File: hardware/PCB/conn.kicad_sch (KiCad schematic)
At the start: 19 parts, among them J3 Motor1, J4 Motor2, J5 Motor3, J6 6V, J7 SJ-3523-SMT-TR, Q1 2N3904, Q2 2N3904, SW3 PWR

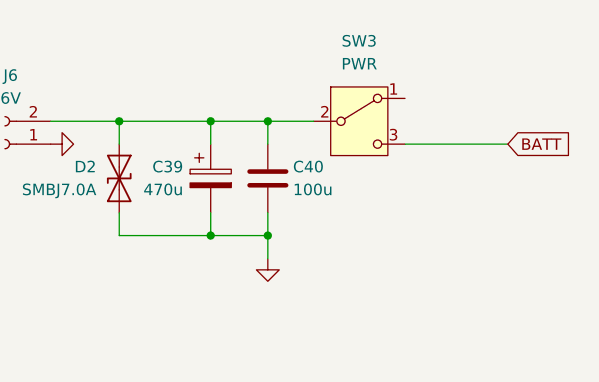
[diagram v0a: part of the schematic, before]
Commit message: Added connection for external IMU to PCB
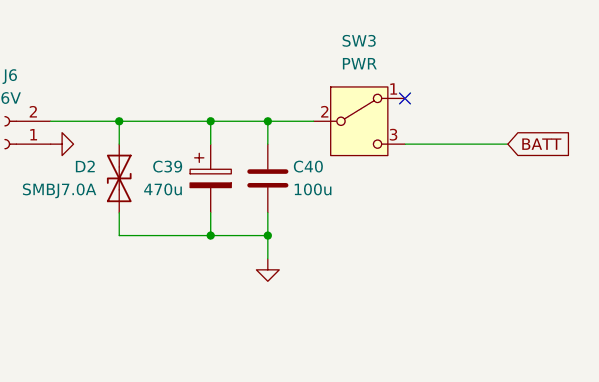
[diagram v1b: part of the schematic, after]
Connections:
- no-connect marks 0 -> 1
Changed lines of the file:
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@@
 		(color 0 0 0 0)
+	)
+	(no_connect
+		(at 173.99 30.48)
 	)
 	(wire

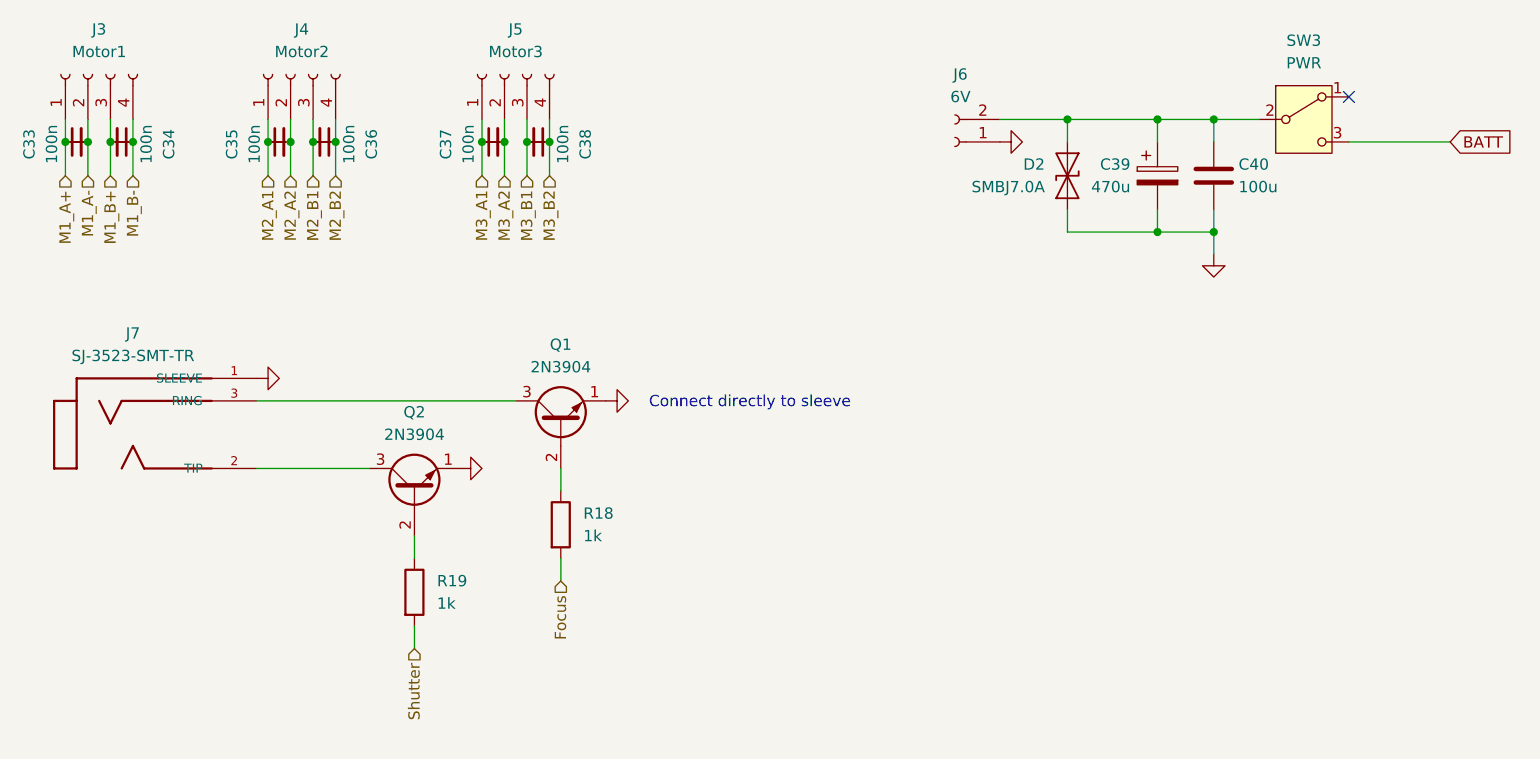
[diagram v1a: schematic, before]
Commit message: Finished schematic for LoRa, added BME280
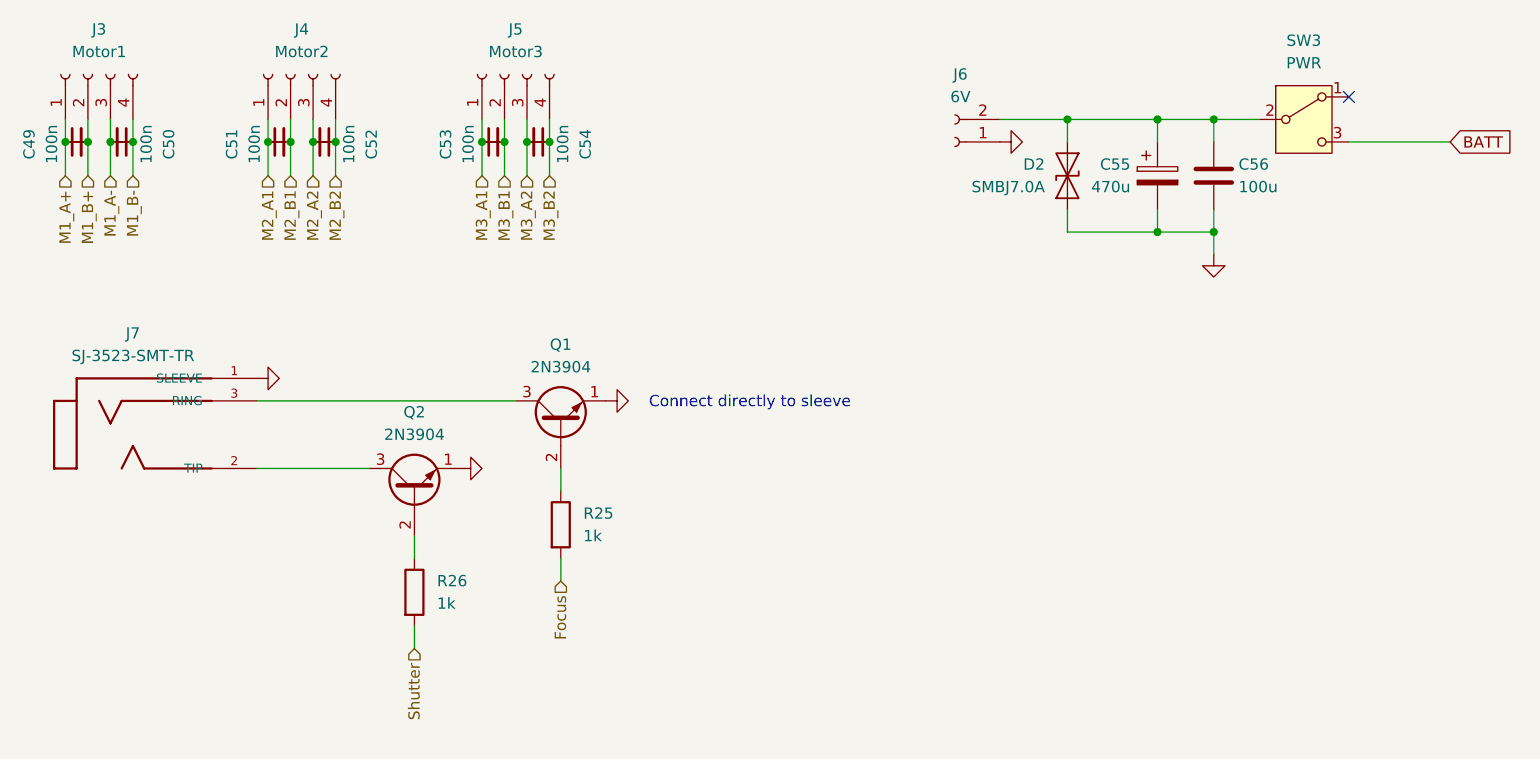
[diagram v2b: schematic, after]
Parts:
- renumbered C33 to C49, C34 to C50, C35 to C51, C36 to C52, C37 to C53, C38 to C54, C39 to C55, C40 to C56, R18 to R25, R19 to R26
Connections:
- net M1_A-: now also C50.2, J3.3 (Pin_3); no longer C49.2, J3.2 (Pin_2)
- net M1_B+: now also C49.2, J3.2 (Pin_2); no longer C50.2, J3.3 (Pin_3)
- net M2_A2: now also C52.2, J4.3 (Pin_3); no longer C51.2, J4.2 (Pin_2)
- net M2_B1: now also C51.2, J4.2 (Pin_2); no longer C52.2, J4.3 (Pin_3)
- net M3_A2: now also C54.2, J5.3 (Pin_3); no longer C53.2, J5.2 (Pin_2)
- net M3_B1: now also C53.2, J5.2 (Pin_2); no longer C54.2, J5.3 (Pin_3)
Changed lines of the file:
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@@
 	(hierarchical_label "M3_A2"
 		(shape input)
-		(at 78.74 39.37 270)
+		(at 81.28 39.37 270)
 		(effects
 			(font
@@
 	(hierarchical_label "M1_B+"
 		(shape input)
-		(at 34.29 39.37 270)
+		(at 31.75 39.37 270)
 		(effects
 			(font
@@
 	(hierarchical_label "M1_A-"
 		(shape input)
-		(at 31.75 39.37 270)
+		(at 34.29 39.37 270)
 		(effects
 			(font
@@
 	(hierarchical_label "M2_A2"
 		(shape input)
-		(at 54.61 39.37 270)
+		(at 57.15 39.37 270)
 		(effects
 			(font
@@
 	(hierarchical_label "M3_B1"
 		(shape input)
-		(at 81.28 39.37 270)
+		(at 78.74 39.37 270)
 		(effects
 			(font
@@
 	(hierarchical_label "M2_B1"
 		(shape input)
-		(at 57.15 39.37 270)
+		(at 54.61 39.37 270)
 		(effects
 			(font
@@
 		(on_board yes)
 		(dnp no)
-		(property "Reference" "C39"
+		(property "Reference" "C55"
 			(at 149.352 38.1 0)
 			(effects
@@
 			(project ""
 				(path "/45ea479c-a8ef-4c14-88b0-391ede4fd156/1d933153-cc32-40aa-bf24-5d7da12d1a94"
-					(reference "C39")
+					(reference "C55")
 					(unit 1)
 				)
@@
 		(on_board yes)
 		(dnp no)
-		(property "Reference" "C36"
+		(property "Reference" "C52"
 			(at 63.754 35.814 0)
 			(effects
@@
 			(project "Startracker"
 				(path "/45ea479c-a8ef-4c14-88b0-391ede4fd156/1d933153-cc32-40aa-bf24-5d7da12d1a94"
-					(reference "C36")
+					(reference "C52")
 					(unit 1)
 				)
@@
 		(on_board yes)
 		(dnp no)
-		(property "Reference" "C40"
+		(property "Reference" "C56"
 			(at 161.544 38.1 0)
 			(effects
@@
 			(project ""
 				(path "/45ea479c-a8ef-4c14-88b0-391ede4fd156/1d933153-cc32-40aa-bf24-5d7da12d1a94"
-					(reference "C40")
+					(reference "C56")
 					(unit 1)
 				)
@@
 		(on_board yes)
 		(dnp no)
-		(property "Reference" "C33"
+		(property "Reference" "C49"
 			(at 25.146 35.814 0)
 			(effects
@@
 			(project ""
 				(path "/45ea479c-a8ef-4c14-88b0-391ede4fd156/1d933153-cc32-40aa-bf24-5d7da12d1a94"
-					(reference "C33")
+					(reference "C49")
 					(unit 1)
 				)
@@
 		(dnp no)
 		(fields_autoplaced yes)
-		(property "Reference" "R18"
+		(property "Reference" "R25"
 			(at 87.63 77.4699 0)
 			(effects
@@
 			(project ""
 				(path "/45ea479c-a8ef-4c14-88b0-391ede4fd156/1d933153-cc32-40aa-bf24-5d7da12d1a94"
-					(reference "R18")
+					(reference "R25")
 					(unit 1)
 				)
@@
 		(dnp no)
 		(fields_autoplaced yes)
-		(property "Reference" "#PWR068"
+		(property "Reference" "#PWR0103"
 			(at 158.75 54.61 0)
 			(effects
@@
 			(project ""
 				(path "/45ea479c-a8ef-4c14-88b0-391ede4fd156/1d933153-cc32-40aa-bf24-5d7da12d1a94"
-					(reference "#PWR068")
+					(reference "#PWR0103")
 					(unit 1)
 				)
@@
 		(on_board yes)
 		(dnp no)
-		(property "Reference" "C34"
+		(property "Reference" "C50"
 			(at 40.894 35.814 0)
 			(effects
@@
 			(project "Startracker"
 				(path "/45ea479c-a8ef-4c14-88b0-391ede4fd156/1d933153-cc32-40aa-bf24-5d7da12d1a94"
-					(reference "C34")
+					(reference "C50")
 					(unit 1)
 				)
@@
 		(dnp no)
 		(fields_autoplaced yes)
-		(property "Reference" "#PWR067"
+		(property "Reference" "#PWR0102"
 			(at 140.97 35.56 0)
 			(effects
@@
 			(project "Startracker"
 				(path "/45ea479c-a8ef-4c14-88b0-391ede4fd156/1d933153-cc32-40aa-bf24-5d7da12d1a94"
-					(reference "#PWR067")
+					(reference "#PWR0102")
 					(unit 1)
 				)
@@
 		(dnp no)
 		(fields_autoplaced yes)
-		(property "Reference" "#PWR070"
+		(property "Reference" "#PWR0105"
 			(at 96.52 64.77 0)
 			(effects
@@
 			(project "Startracker"
 				(path "/45ea479c-a8ef-4c14-88b0-391ede4fd156/1d933153-cc32-40aa-bf24-5d7da12d1a94"
-					(reference "#PWR070")
+					(reference "#PWR0105")
 					(unit 1)
 				)
@@
 		(dnp no)
 		(fields_autoplaced yes)
-		(property "Reference" "#PWR071"
+		(property "Reference" "#PWR0106"
 			(at 80.01 72.39 0)
 			(effects
@@
 			(project "Startracker"
 				(path "/45ea479c-a8ef-4c14-88b0-391ede4fd156/1d933153-cc32-40aa-bf24-5d7da12d1a94"
-					(reference "#PWR071")
+					(reference "#PWR0106")
 					(unit 1)
 				)
@@
 		(dnp no)
 		(fields_autoplaced yes)
-		(property "Reference" "#PWR069"
+		(property "Reference" "#PWR0104"
 			(at 57.15 62.23 0)
 			(effects
@@
 			(project "Startracker"
 				(path "/45ea479c-a8ef-4c14-88b0-391ede4fd156/1d933153-cc32-40aa-bf24-5d7da12d1a94"
-					(reference "#PWR069")
+					(reference "#PWR0104")
 					(unit 1)
 				)
@@
 		(on_board yes)
 		(dnp no)
-		(property "Reference" "C35"
+		(property "Reference" "C51"
 			(at 48.006 35.814 0)
 			(effects
@@
 			(project "Startracker"
 				(path "/45ea479c-a8ef-4c14-88b0-391ede4fd156/1d933153-cc32-40aa-bf24-5d7da12d1a94"
-					(reference "C35")
+					(reference "C51")
 					(unit 1)
 				)
@@
 		(on_board yes)
 		(dnp no)
-		(property "Reference" "C37"
+		(property "Reference" "C53"
 			(at 72.136 35.814 0)
 			(effects
@@
 			(project "Startracker"
 				(path "/45ea479c-a8ef-4c14-88b0-391ede4fd156/1d933153-cc32-40aa-bf24-5d7da12d1a94"
-					(reference "C37")
+					(reference "C53")
 					(unit 1)
 				)
@@
 		(on_board yes)
 		(dnp no)
-		(property "Reference" "C38"
+		(property "Reference" "C54"
 			(at 87.884 35.814 0)
 			(effects
@@
 			(project "Startracker"
 				(path "/45ea479c-a8ef-4c14-88b0-391ede4fd156/1d933153-cc32-40aa-bf24-5d7da12d1a94"
-					(reference "C38")
+					(reference "C54")
 					(unit 1)
 				)
@@
 		(dnp no)
 		(fields_autoplaced yes)
-		(property "Reference" "R19"
+		(property "Reference" "R26"
 			(at 71.12 85.0899 0)
 			(effects
@@
 			(project "Startracker"
 				(path "/45ea479c-a8ef-4c14-88b0-391ede4fd156/1d933153-cc32-40aa-bf24-5d7da12d1a94"
-					(reference "R19")
-					(unit 1)
-				)
+					(reference "R26")
+					(unit 1)
+				)

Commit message: Finished parts sourcing and added missing footprints
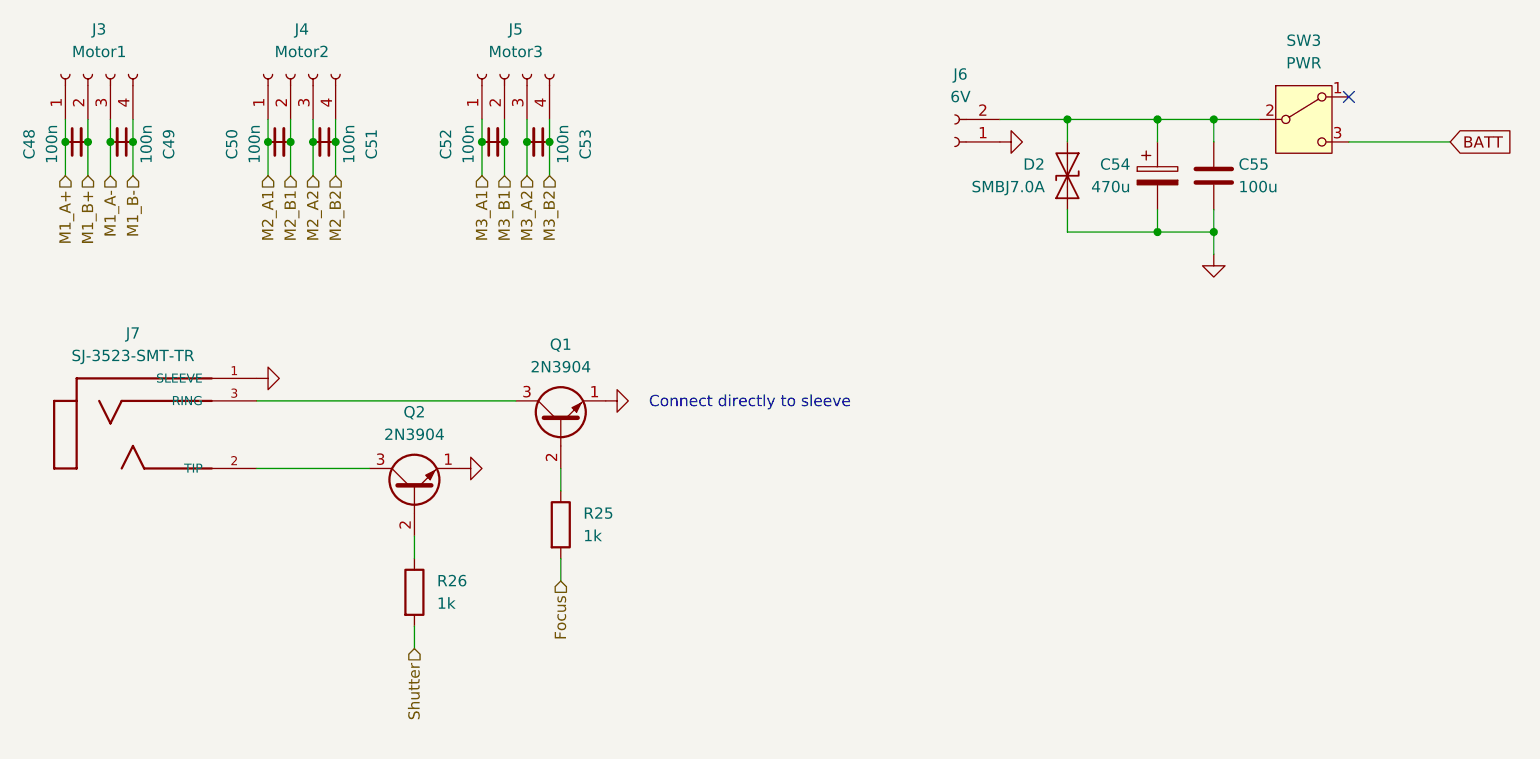
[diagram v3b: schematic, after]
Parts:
- renumbered C49 to C48, C50 to C49, C51 to C50, C52 to C51, C53 to C52, C54 to C53, C55 to C54, C56 to C55
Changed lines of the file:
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@@
 		(on_board yes)
 		(dnp no)
-		(property "Reference" "C55"
+		(property "Reference" "C54"
 			(at 149.352 38.1 0)
 			(effects
@@
 			(project ""
 				(path "/45ea479c-a8ef-4c14-88b0-391ede4fd156/1d933153-cc32-40aa-bf24-5d7da12d1a94"
-					(reference "C55")
+					(reference "C54")
 					(unit 1)
 				)
@@
 		(on_board yes)
 		(dnp no)
-		(property "Reference" "C52"
+		(property "Reference" "C51"
 			(at 63.754 35.814 0)
 			(effects
@@
 			(project "Startracker"
 				(path "/45ea479c-a8ef-4c14-88b0-391ede4fd156/1d933153-cc32-40aa-bf24-5d7da12d1a94"
-					(reference "C52")
+					(reference "C51")
 					(unit 1)
 				)
@@
 		(on_board yes)
 		(dnp no)
-		(property "Reference" "C56"
+		(property "Reference" "C55"
 			(at 161.544 38.1 0)
 			(effects
@@
 			(project ""
 				(path "/45ea479c-a8ef-4c14-88b0-391ede4fd156/1d933153-cc32-40aa-bf24-5d7da12d1a94"
-					(reference "C56")
+					(reference "C55")
 					(unit 1)
 				)
@@
 		(on_board yes)
 		(dnp no)
-		(property "Reference" "C49"
+		(property "Reference" "C48"
 			(at 25.146 35.814 0)
 			(effects
@@
 			(project ""
 				(path "/45ea479c-a8ef-4c14-88b0-391ede4fd156/1d933153-cc32-40aa-bf24-5d7da12d1a94"
-					(reference "C49")
+					(reference "C48")
 					(unit 1)
 				)
@@
 		(on_board yes)
 		(dnp no)
-		(property "Reference" "C50"
+		(property "Reference" "C49"
 			(at 40.894 35.814 0)
 			(effects
@@
 			(project "Startracker"
 				(path "/45ea479c-a8ef-4c14-88b0-391ede4fd156/1d933153-cc32-40aa-bf24-5d7da12d1a94"
-					(reference "C50")
+					(reference "C49")
 					(unit 1)
 				)
@@
 		(on_board yes)
 		(dnp no)
-		(property "Reference" "C51"
+		(property "Reference" "C50"
 			(at 48.006 35.814 0)
 			(effects
@@
 			(project "Startracker"
 				(path "/45ea479c-a8ef-4c14-88b0-391ede4fd156/1d933153-cc32-40aa-bf24-5d7da12d1a94"
-					(reference "C51")
+					(reference "C50")
 					(unit 1)
 				)
@@
 		(on_board yes)
 		(dnp no)
-		(property "Reference" "C53"
+		(property "Reference" "C52"
 			(at 72.136 35.814 0)
 			(effects
@@
 			(project "Startracker"
 				(path "/45ea479c-a8ef-4c14-88b0-391ede4fd156/1d933153-cc32-40aa-bf24-5d7da12d1a94"
-					(reference "C53")
+					(reference "C52")
 					(unit 1)
 				)
@@
 		(on_board yes)
 		(dnp no)
-		(property "Reference" "C54"
+		(property "Reference" "C53"
 			(at 87.884 35.814 0)
 			(effects
@@
 			(project "Startracker"
 				(path "/45ea479c-a8ef-4c14-88b0-391ede4fd156/1d933153-cc32-40aa-bf24-5d7da12d1a94"
-					(reference "C54")
-					(unit 1)
-				)
+					(reference "C53")
+					(unit 1)
+				)

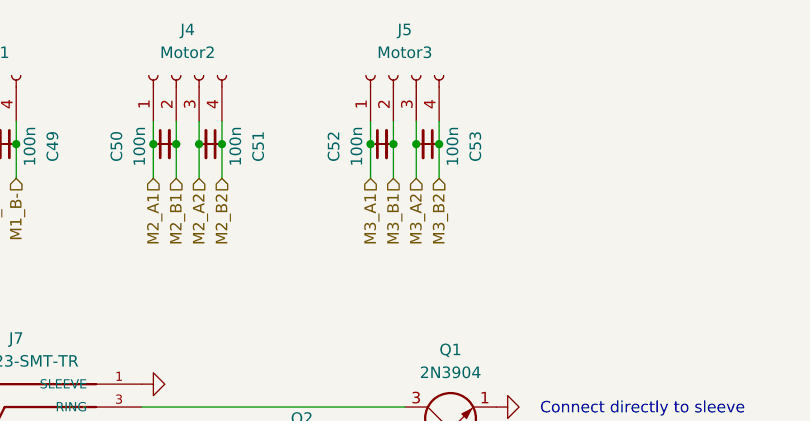
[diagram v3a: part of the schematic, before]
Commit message: Removed polar azimuth motor driver from pcb
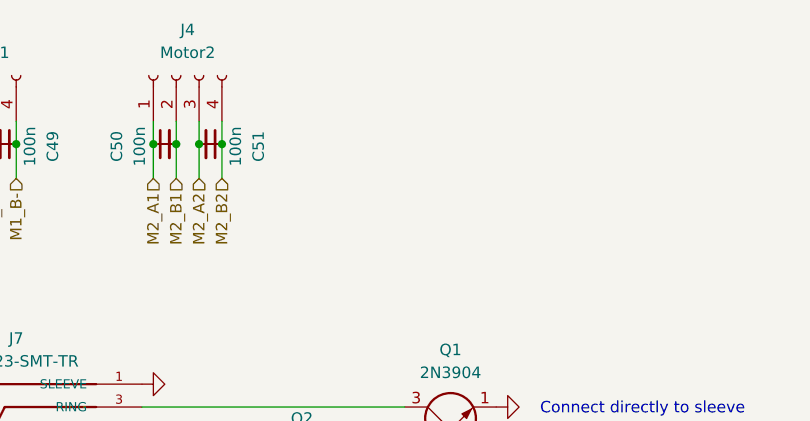
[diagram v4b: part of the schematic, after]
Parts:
- removed C52, C53: 100n, Capacitor_SMD:C_1206_3216Metric_Pad1.33x1.80mm_HandSolder, symbol saját:C_Super_Small
- removed J5: Motor3, Connector_JST:JST_XH_B4B-XH-A_1x04_P2.50mm_Vertical, symbol Connector:Conn_01x04_Socket
